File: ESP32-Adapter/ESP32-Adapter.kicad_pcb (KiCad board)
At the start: 2 copper layers, 65.4 x 87.8 mm, 21 parts, among them J10 Barrel_Jack, J12 Conn_01x05, J13 Conn_01x05, J2 Conn_01x03, J3 Conn_01x03, J5 Conn_01x03, U1 ESP32-C5-DevKitC-1, U2 LM317DCYR, U3 Adafruit CANPAL, U4 ADAFRUIT INA219 BREAKOUT

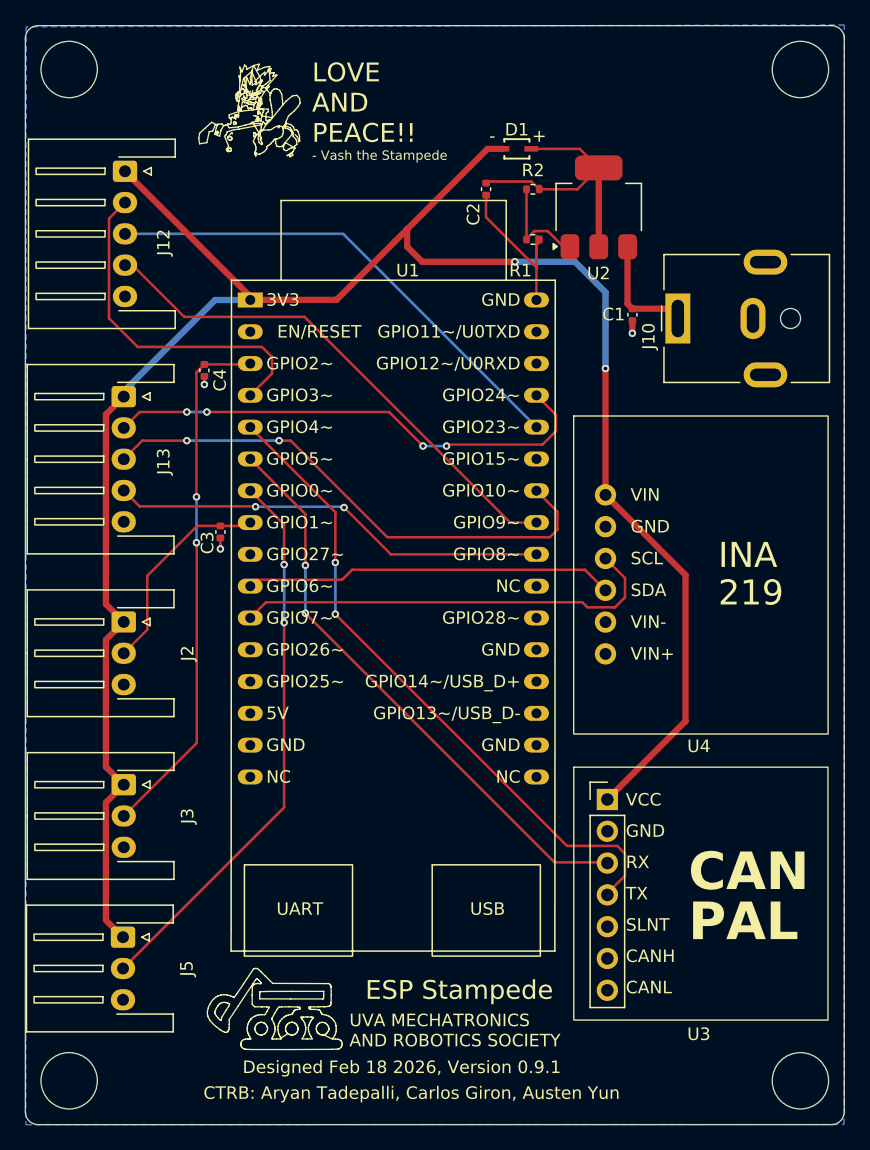
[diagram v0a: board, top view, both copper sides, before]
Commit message: Add port labels
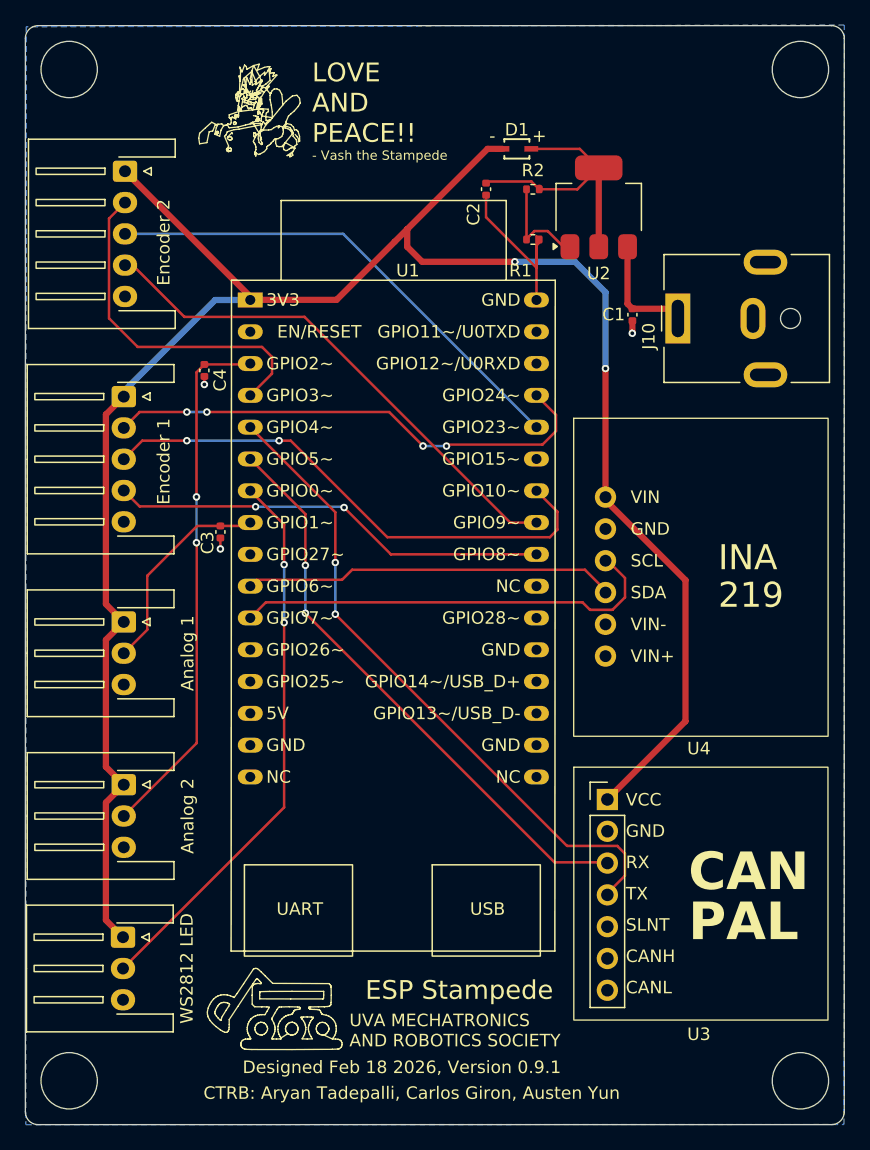
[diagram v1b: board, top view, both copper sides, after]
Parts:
- Analog 1: renamed from J2
- Analog 2: renamed from J3
- Encoder 1: renamed from J13
- Encoder 2: renamed from J12
- WS2812 LED: renamed from J5
- moved U4 0.18 mm to (123.6, 68.6)
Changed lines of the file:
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@@
 	(footprint "footprints:INA219 Breakout"
 		(layer "F.Cu")
-		(at 123.6109 68.42)
+		(at 123.6109 68.6)
 		(property "Reference" "U4"
 			(at 7.46 20.08 0)
@@
 		(descr "JST XH series connector, S3B-XH-A-1 (http://www.jst-mfg.com/product/pdf/eng/eXH.pdf), generated with kicad-footprint-generator")
 		(tags "connector JST XH horizontal")
-		(property "Reference" "J2"
+		(property "Reference" "Analog 1"
 			(at 2.5 -5.1 90)
 			(layer "F.SilkS")
@@
 		(descr "JST XH series connector, S3B-XH-A-1 (http://www.jst-mfg.com/product/pdf/eng/eXH.pdf), generated with kicad-footprint-generator")
 		(tags "connector JST XH horizontal")
-		(property "Reference" "J5"
+		(property "Reference" "WS2812 LED"
 			(at 2.5 -5.1 90)
 			(layer "F.SilkS")
@@
 		(descr "JST XH series connector, S5B-XH-A-1 (http://www.jst-mfg.com/product/pdf/eng/eXH.pdf), generated with kicad-footprint-generator")
 		(tags "connector JST XH horizontal")
-		(property "Reference" "J13"
+		(property "Reference" "Encoder 1"
 			(at 5.18 -3.19 90)
 			(layer "F.SilkS")
@@
 		(descr "JST XH series connector, S5B-XH-A-1 (http://www.jst-mfg.com/product/pdf/eng/eXH.pdf), generated with kicad-footprint-generator")
 		(tags "connector JST XH horizontal")
-		(property "Reference" "J12"
+		(property "Reference" "Encoder 2"
 			(at 5.68 -3.09 90)
 			(layer "F.SilkS")
@@
 		(descr "JST XH series connector, S3B-XH-A-1 (http://www.jst-mfg.com/product/pdf/eng/eXH.pdf), generated with kicad-footprint-generator")
 		(tags "connector JST XH horizontal")
-		(property "Reference" "J3"
+		(property "Reference" "Analog 2"
 			(at 2.5 -5.1 90)
 			(layer "F.SilkS")
@@
 	)
 	(segment
-		(start 130.0009 74.82)
-		(end 130.0009 86.5)
+		(start 123.6109 68.84)
+		(end 130.0009 75.23)
 		(width 0.5)
 		(layer "F.Cu")
@@
 	)
 	(segment
+		(start 130.0009 86.5)
+		(end 123.7309 92.77)
+		(width 0.5)
+		(layer "F.Cu")
+		(net 6)
+	)
+	(segment
 		(start 116.3709 49.8)
 		(end 108.9709 49.8)
@@
 	)
 	(segment
+		(start 123.6109 58.328591)
+		(end 123.6109 68.84)
+		(width 0.5)
+		(layer "F.Cu")
+		(net 6)
+	)
+	(segment
 		(start 114.1909 40.78)
 		(end 107.7709 47.2)
@@
 	)
 	(segment
-		(start 107.7709 48.6)
-		(end 107.7709 47.2)
+		(start 130.0009 75.23)
+		(end 130.0009 86.5)
 		(width 0.5)
 		(layer "F.Cu")
@@
 	)
 	(segment
-		(start 123.6109 68.42)
-		(end 123.6109 58.328591)
+		(start 107.7709 48.6)
+		(end 107.7709 47.2)
 		(width 0.5)
 		(layer "F.Cu")
@@
 	)
 	(segment
-		(start 130.0009 86.5)
-		(end 123.7309 92.77)
-		(width 0.5)
-		(layer "F.Cu")
-		(net 6)
-	)
-	(segment
 		(start 85.1309 78.57)
 		(end 83.7049 77.144)
@@
 	)
 	(segment
-		(start 123.6109 68.43)
-		(end 130.0009 74.82)
-		(width 0.5)
-		(layer "F.Cu")
-		(net 6)
-	)
-	(segment
 		(start 95.2377 52.5768)
 		(end 95.2377 52.85032)
@@
 	)
 	(segment
-		(start 123.6109 68.42)
-		(end 123.6109 68.43)
-		(width 0.5)
-		(layer "F.Cu")
-		(net 6)
-	)
-	(segment
 		(start 85.1309 78.57)
 		(end 83.7049 79.996)
@@
 	)
 	(segment
-		(start 102.5709 75.2)
-		(end 103.3709 74.4)
+		(start 103.3709 74.4)
+		(end 121.9709 74.4)
+		(width 0.2032)
+		(layer "F.Cu")
+		(net 13)
+	)
+	(segment
+		(start 95.74802 75.2)
+		(end 102.5709 75.2)
 		(width 0.2032)
 		(layer "F.Cu")
@@
 	)
 	(segment
-		(start 103.3709 74.4)
-		(end 121.9709 74.4)
+		(start 123.6109 76.04)
+		(end 123.6109 76.22)
 		(width 0.2032)
 		(layer "F.Cu")
@@
 	)
 	(segment
-		(start 95.74802 75.2)
-		(end 102.5709 75.2)
+		(start 102.5709 75.2)
+		(end 103.3709 74.4)
 		(width 0.2032)
 		(layer "F.Cu")
@@
 	)
 	(segment
-		(start 96.48802 77)
-		(end 121.7709 77)
+		(start 124.1709 77.6)
+		(end 125.1709 76.6)
 		(width 0.2032)
 		(layer "F.Cu")
@@
 	)
 	(segment
-		(start 124.3709 77.4)
-		(end 125.1709 76.6)
+		(start 95.2377 78.25032)
+		(end 96.48802 77)
 		(width 0.2032)
 		(layer "F.Cu")
@@
 	)
 	(segment
-		(start 95.2377 78.25032)
-		(end 96.48802 77)
+		(start 96.48802 77)
+		(end 121.7709 77)
 		(width 0.2032)
 		(layer "F.Cu")
@@
 	)
 	(segment
-		(start 125.1709 75.06)
-		(end 123.6109 73.5)
+		(start 121.7709 77)
+		(end 122.3709 77.6)
 		(width 0.2032)
 		(layer "F.Cu")
@@
 	)
 	(segment
-		(start 121.7709 77)
-		(end 122.1709 77.4)
+		(start 125.1709 76.6)
+		(end 125.1709 75.06)
 		(width 0.2032)
 		(layer "F.Cu")
@@
 	)
 	(segment
-		(start 122.1709 77.4)
-		(end 124.3709 77.4)
+		(start 125.1709 75.06)
+		(end 123.6109 73.5)
 		(width 0.2032)
 		(layer "F.Cu")
@@
 	)
 	(segment
-		(start 125.1709 76.6)
-		(end 125.1709 75.06)
+		(start 122.3709 77.6)
+		(end 124.1709 77.6)
 		(width 0.2032)
 		(layer "F.Cu")

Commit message: generate gerbers
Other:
- board text added: "Designed Feb 18 2026, Version 1.0"
- board text removed: "Designed Feb 18 2026, Version 0.9.1"
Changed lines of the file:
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@@
 			(plot_on_all_layers_selection 0x00000000_00000000_00000000_00000000)
 			(disableapertmacros no)
-			(usegerberextensions no)
+			(usegerberextensions yes)
 			(usegerberattributes yes)
 			(usegerberadvancedattributes yes)
@@
 			(outputformat 1)
 			(mirror no)
-			(drillshape 1)
+			(drillshape 0)
 			(scaleselection 1)
-			(outputdirectory "")
+			(outputdirectory "v1.0_Gerbers/")
 		)
 	)
@@
 		)
 	)
-	(gr_text "Designed Feb 18 2026, Version 0.9.1\n"
+	(gr_text "Designed Feb 18 2026, Version 1.0\n"
 		(at 107.3409 114.14 0)
 		(layer "F.SilkS")

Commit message: retracing for proper gpio layout
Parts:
- J12: renamed from Encoder 2
- J13: renamed from Encoder 1
- J2: renamed from Analog 1
- J3: renamed from Analog 2
- J5: renamed from WS2812 LED
- U1: footprint footprints:ESP32-C5-DevKitC-1 -> PCM_Espressif:ESP32-C5-DevKitC-1
- moved C3 12.3 mm to (91.8, 59.1)
- moved C4 3.41 mm to (91.8, 61.9)
- moved U1 0.92 mm to (94.7, 53.6)
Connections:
- U1 pad 10: /I2C SDA -> /I2C SCL
- U1 pad 11: /I2C SCL -> /I2C SDA
- U1 pad 24: /IDX1 -> /CAN RX
- U1 pad 25: /IDX2 -> /CAN TX
- U1 pad 26: /A1 -> /A2
- U1 pad 27: unconnected-(U1-GPIO15-Pad27) -> /B2
- U1 pad 28: /A2 -> unconnected-(U1-GPIO23-Pad28)
- U1 pad 29: /B1 -> unconnected-(U1-GPIO24-Pad29)
- U1 pad 3: /SIG2 -> /SIG1
- U1 pad 4: /B2 -> /SIG2
- U1 pad 5: /CAN TX -> /B1
- U1 pad 6: /CAN RX -> /A1
- U1 pad 8: /SIG1 -> /IDX2
- U1 pad 9: unconnected-(U1-GPIO27-Pad9) -> /IDX1
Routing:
- net /A1: track 42.6 -> 9.97 mm, vias 2 -> 0
- net /B1: track 40.3 -> 10.9 mm, vias 4 -> 0
- net /IDX1: track 35.1 -> 12.0 mm, vias 2 -> 0
- net /B2: track 27.9 -> 46.3 mm, vias 0 -> 3
- net /SIG1: track 17.1 -> 28.2 mm
- net /CAN RX: track 46.5 -> 36.6 mm
- net GND: track 17.1 -> 26.5 mm
- net /CAN TX: track 52.6 -> 43.7 mm
- net /A2: track 39.3 -> 46.6 mm, vias 0 -> 3
- net /SIG2: track 42.4 -> 38.4 mm, vias 2 -> 0
- net /I2C SCL: track 34.9 -> 31.1 mm
- net /IDX2: track 42.0 -> 45.5 mm, vias 0 -> 4
- net /WS2812: track 44.6 -> 41.4 mm, vias 2 -> 0
- net +3.3V: track 164.3 -> 166.6 mm
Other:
- board text added: "Designed Mar 19 2026, Version 2.0"
- board text added: "GPIO12~/U0RXD"
- board text removed: "Designed Feb 18 2026, Version 1.0"
